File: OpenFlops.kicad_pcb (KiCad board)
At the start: 2 copper layers, 112 x 59.3 mm, 74 parts, among them P1 FLOPPY_CONN, P2 POWER_INPUT, P3 USB_A_FEMALE, P4 PROG_PORT, P5 JUMPERS, P6 ENCODER_PORT, P7 DISPLAY_PORT, Q1 MOS_N_GSD, Q2 MOS_N_GSD, Q3 MOS_N_GSD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

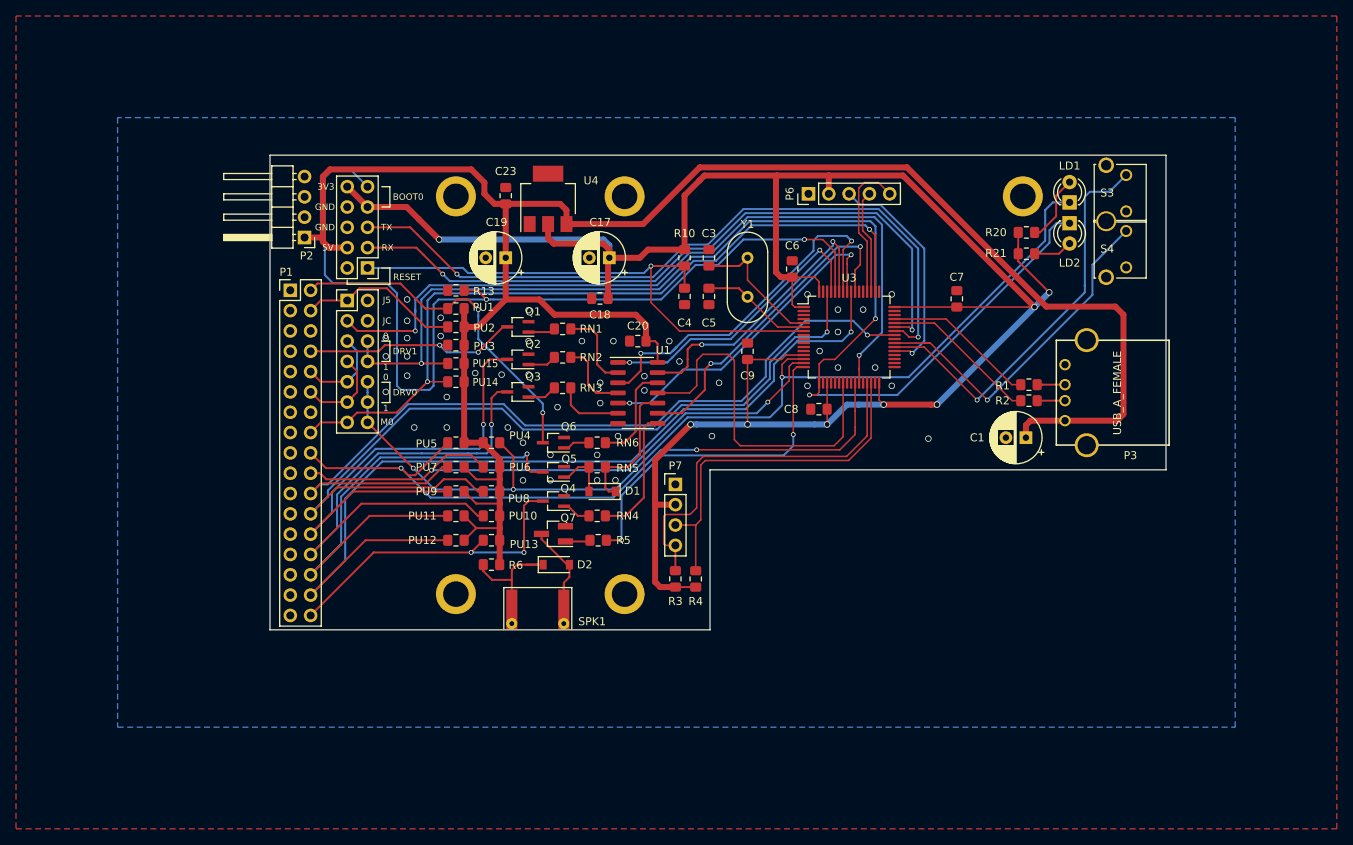
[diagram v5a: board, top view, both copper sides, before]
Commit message: Add P6/P7 pin names
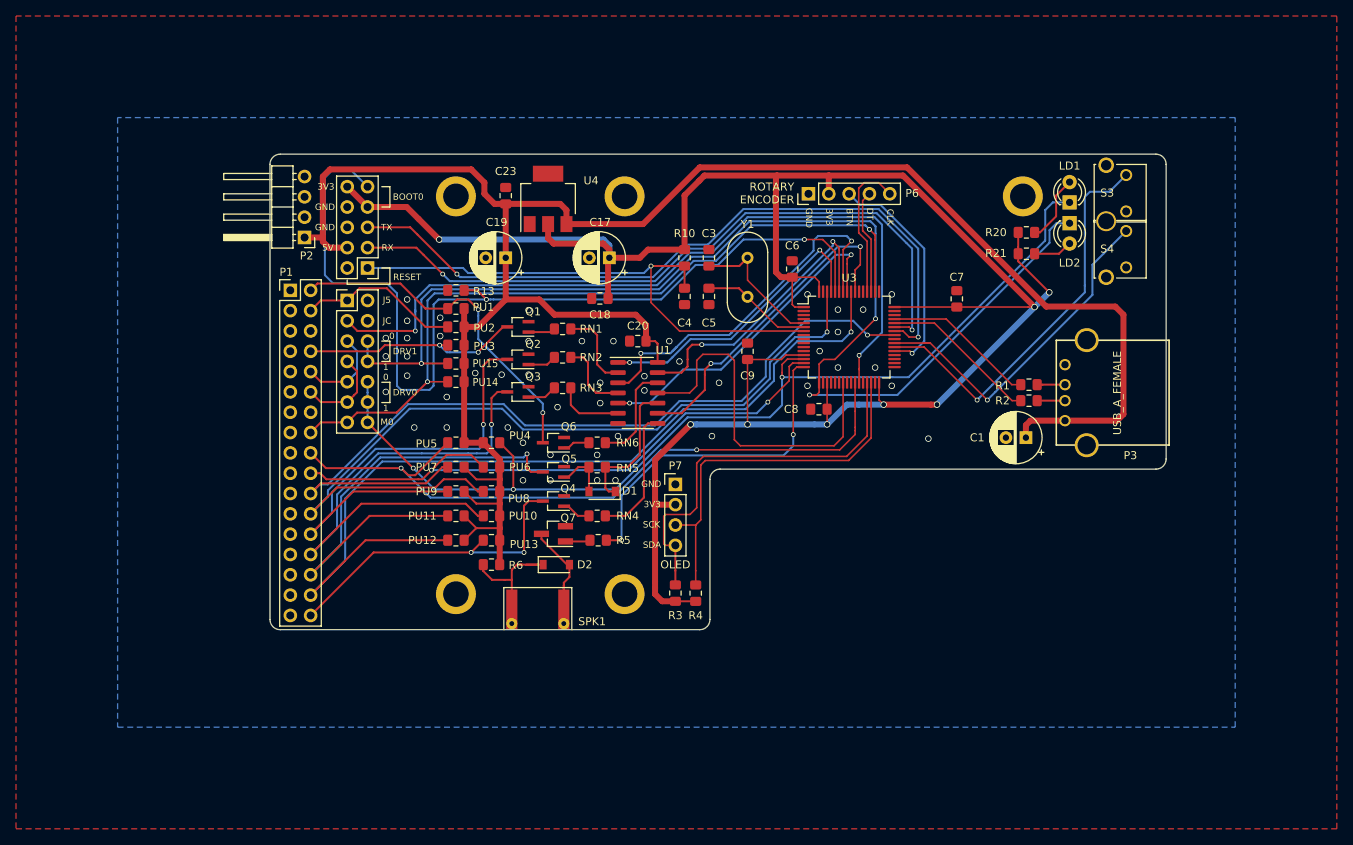
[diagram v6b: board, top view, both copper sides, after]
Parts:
- moved R3 1.78 mm to (145.9, 110.2)
- moved R4 1.78 mm to (148.5, 110.2)
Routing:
- net /disp_clk: track 45.6 -> 47.4 mm
- net /disp_dio: track 47.7 -> 49.5 mm
- net +3V3: track 280.2 -> 281.7 mm
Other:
- board size 112 x 59.3 mm -> 112 x 59.4 mm
- board text added: "BTN"
- board text added: "CLK"
- board text added: "DT"
- board text added: "OLED"
- board text added: "ROTARY ENCODER"
- board text added: "SCK"
- board text added: "SDA"
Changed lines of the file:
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@@
   (general
     (thickness 1.6)
-    (drawings 39)
-    (tracks 823)
+    (drawings 57)
+    (tracks 826)
     (zones 0)
     (modules 74)
@@
     (user_trace_width 0.25)
     (trace_clearance 0.25)
-    (zone_clearance 0.000254)
+    (zone_clearance 0.254)
     (zone_45_only no)
     (trace_min 0.16)
@@
     (tags SOD-123)
     (attr smd)
-    (fp_text reference D1 (at -3.81 0.066668) (layer F.SilkS)
+    (fp_text reference D1 (at -3.439 0.066668) (layer F.SilkS)
       (effects (font (size 1 1) (thickness 0.15)))
     )
@@
   )
   (module Resistor_SMD:R_0805_2012Metric_Pad1.15x1.40mm_HandSolder (layer F.Cu)
-    (at 145.923 108.458 90)
+    (at 145.923 110.236 90)
     (descr "Resistor SMD 0805 (2012 Metric), square (rectangular) end terminal, IPC_7351 nominal with elongated pad for handsoldering. (Body size source: https://docs.google.com/spreadsheets/d/1BsfQQcO9C6DZCsRaXUlFlo91Tg2WpOkGARC1WS5S8t0/edit?usp=sharing), generated with kicad-footprint-generator")
     (tags "resistor handsolder")
@@
   )
   (module Resistor_SMD:R_0805_2012Metric_Pad1.15x1.40mm_HandSolder (layer F.Cu)
-    (at 148.463 108.467 90)
+    (at 148.463 110.245 90)
     (descr "Resistor SMD 0805 (2012 Metric), square (rectangular) end terminal, IPC_7351 nominal with elongated pad for handsoldering. (Body size source: https://docs.google.com/spreadsheets/d/1BsfQQcO9C6DZCsRaXUlFlo91Tg2WpOkGARC1WS5S8t0/edit?usp=sharing), generated with kicad-footprint-generator")
     (tags "resistor handsolder")
@@
     (descr "Through hole straight pin header, 1x05, 2.54mm pitch, single row")
     (tags "Through hole pin header THT 1x05 2.54mm single row")
-    (fp_text reference P6 (at 0 -2.33 90) (layer F.SilkS)
+    (fp_text reference P6 (at 0.0675 12.954 180) (layer F.SilkS)
       (effects (font (size 1 1) (thickness 0.15)))
     )
@@
     )
   )
+  (gr_text OLED (at 145.923 106.68) (layer F.SilkS)
+    (effects (font (size 1 1) (thickness 0.15)))
+  )
+  (gr_text "ROTARY\nENCODER" (at 160.782 60.2575) (layer F.SilkS)
+    (effects (font (size 1 1) (thickness 0.15)) (justify right))
+  )
+  (gr_text SDA (at 143.002 104.213) (layer F.SilkS)
+    (effects (font (size 0.8 0.8) (thickness 0.12)))
+  )
+  (gr_text SCK (at 142.944857 101.673) (layer F.SilkS)
+    (effects (font (size 0.8 0.8) (thickness 0.12)))
+  )
+  (gr_text 3V3 (at 143.021048 99.133) (layer F.SilkS)
+    (effects (font (size 0.8 0.8) (thickness 0.12)))
+  )
+  (gr_text GND (at 142.906762 96.593) (layer F.SilkS)
+    (effects (font (size 0.8 0.8) (thickness 0.12)))
+  )
+  (gr_text GND (at 162.614 63.341238 270) (layer F.SilkS)
+    (effects (font (size 0.8 0.8) (thickness 0.12)))
+  )
+  (gr_text 3V3 (at 165.154 63.226953 270) (layer F.SilkS)
+    (effects (font (size 0.8 0.8) (thickness 0.12)))
+  )
+  (gr_text BTN (at 167.694 63.246 270) (layer F.SilkS)
+    (effects (font (size 0.8 0.8) (thickness 0.12)))
+  )
+  (gr_text DT (at 170.234 62.826953 270) (layer F.SilkS)
+    (effects (font (size 0.8 0.8) (thickness 0.12)))
+  )
+  (gr_text CLK (at 172.774 63.246 270) (layer F.SilkS)
+    (effects (font (size 0.8 0.8) (thickness 0.12)))
+  )
+  (gr_arc (start 151.511 96.012) (end 151.511 94.742) (angle -90) (layer Edge.Cuts) (width 0.05))
+  (gr_arc (start 96.52 113.538) (end 95.25 113.538) (angle -90) (layer Edge.Cuts) (width 0.05))
+  (gr_arc (start 148.971 113.538) (end 148.971 114.808) (angle -90) (layer Edge.Cuts) (width 0.05))
+  (gr_arc (start 205.994 93.472) (end 205.994 94.742) (angle -90) (layer Edge.Cuts) (width 0.05))
+  (gr_arc (start 205.994 56.642) (end 207.264 56.642) (angle -90) (layer Edge.Cuts) (width 0.05))
+  (gr_arc (start 96.52 56.642) (end 96.52 55.372) (angle -90) (layer Edge.Cuts) (width 0.05))
+  (dimension 112.014 (width 0.15) (layer F.Fab)
+    (gr_text "112,014 mm" (at 151.257 43.022994) (layer F.Fab)
+      (effects (font (size 1 1) (thickness 0.15)))
+    )
+    (feature1 (pts (xy 207.264 55.372) (xy 207.264 43.736573)))
+    (feature2 (pts (xy 95.25 55.372) (xy 95.25 43.736573)))
+    (crossbar (pts (xy 95.25 44.322994) (xy 207.264 44.322994)))
+    (arrow1a (pts (xy 207.264 44.322994) (xy 206.137496 44.909415)))
+    (arrow1b (pts (xy 207.264 44.322994) (xy 206.137496 43.736573)))
+    (arrow2a (pts (xy 95.25 44.322994) (xy 96.376504 44.909415)))
+    (arrow2b (pts (xy 95.25 44.322994) (xy 96.376504 43.736573)))
+  )
   (gr_text M0 (at 109.874238 88.846) (layer F.SilkS)
     (effects (font (size 0.8 0.8) (thickness 0.12)))
@@
     (effects (font (size 0.8 0.8) (thickness 0.12)))
   )
-  (gr_text 0 (at 109.728 78.105) (layer F.SilkS)
+  (gr_text 0 (at 110.49 78.105) (layer F.SilkS)
     (effects (font (size 0.8 0.8) (thickness 0.12)))
   )
@@
     (effects (font (size 0.8 0.8) (thickness 0.12)))
   )
-  (gr_line (start 150.25 94.828) (end 207.25 94.828) (layer Edge.Cuts) (width 0.05))
-  (gr_line (start 150.25 114.828) (end 150.25 94.828) (layer Edge.Cuts) (width 0.05))
-  (gr_line (start 95.25 114.828) (end 150.25 114.828) (layer Edge.Cuts) (width 0.05))
-  (gr_line (start 207.25 55.5) (end 207.25 94.828) (layer Edge.Cuts) (width 0.05))
-  (gr_line (start 95.25 55.5) (end 207.25 55.5) (layer Edge.Cuts) (width 0.05))
-  (gr_line (start 95.25 55.5) (end 95.25 114.828) (layer Edge.Cuts) (width 0.05))
+  (gr_line (start 151.511 94.742) (end 205.994 94.742) (layer Edge.Cuts) (width 0.05))
+  (gr_line (start 150.241 113.538) (end 150.241 96.012) (layer Edge.Cuts) (width 0.05))
+  (gr_line (start 96.52 114.808) (end 148.971 114.808) (layer Edge.Cuts) (width 0.05))
+  (gr_line (start 207.264 56.642) (end 207.264 93.472) (layer Edge.Cuts) (width 0.05))
+  (gr_line (start 96.52 55.372) (end 205.994 55.372) (layer Edge.Cuts) (width 0.05))
+  (gr_line (start 95.25 56.642) (end 95.25 113.538) (layer Edge.Cuts) (width 0.05))
   (via (at 177.546 90.932) (size 0.8) (drill 0.6) (layers F.Cu B.Cu) (net 1))
   (via (at 124.968 89.535) (size 0.8) (drill 0.6) (layers F.Cu B.Cu) (net 1))
@@
   (via (at 120.904 82.733806) (size 0.8) (drill 0.6) (layers F.Cu B.Cu) (net 1))
   (via (at 109.728 85.09) (size 0.8) (drill 0.6) (layers F.Cu B.Cu) (net 1))
-  (via (at 116.586 75.819) (size 0.8) (drill 0.6) (layers F.Cu B.Cu) (net 1))
-  (via (at 116.586 78.105) (size 0.8) (drill 0.6) (layers F.Cu B.Cu) (net 1))
+  (via (at 116.5225 75.819) (size 0.8) (drill 0.6) (layers F.Cu B.Cu) (net 1))
+  (via (at 116.5225 78.105) (size 0.8) (drill 0.6) (layers F.Cu B.Cu) (net 1))
   (via (at 112.395 73.533) (size 0.8) (drill 0.6) (layers F.Cu B.Cu) (net 1))
   (via (at 112.395 76.2) (size 0.8) (drill 0.6) (layers F.Cu B.Cu) (net 1))
@@
   (segment (start 104.902 59.436) (end 107.442 61.976) (width 0.75) (layer F.Cu) (net 5))
   (segment (start 143.383 93.599) (end 143.383 98.425) (width 0.75) (layer F.Cu) (net 5))
-  (segment (start 148.454 109.483) (end 148.463 109.492) (width 0.25) (layer F.Cu) (net 5))
-  (segment (start 145.923 109.483) (end 148.454 109.483) (width 0.25) (layer F.Cu) (net 5))
-  (segment (start 144.027 109.483) (end 145.923 109.483) (width 0.75) (layer F.Cu) (net 5))
-  (segment (start 143.383 108.839) (end 144.027 109.483) (width 0.75) (layer F.Cu) (net 5))
   (segment (start 143.383 99.187) (end 145.923 99.187) (width 0.75) (layer F.Cu) (net 5))
   (segment (start 143.383 98.425) (end 143.383 99.187) (width 0.75) (layer F.Cu) (net 5))
@@
   (via (at 178.6255 86.6775) (size 0.8) (drill 0.6) (layers F.Cu B.Cu) (net 5))
   (segment (start 177.8635 86.6775) (end 178.6255 86.6775) (width 0.75) (layer F.Cu) (net 5))
+  (segment (start 145.923 111.261) (end 148.333593 111.261) (width 0.25) (layer F.Cu) (net 5))
+  (segment (start 143.383 109.601) (end 143.383 110.363) (width 0.75) (layer F.Cu) (net 5))
+  (segment (start 143.383 108.839) (end 143.383 109.601) (width 0.75) (layer F.Cu) (net 5))
+  (segment (start 144.281 111.261) (end 145.923 111.261) (width 0.75) (layer F.Cu) (net 5))
+  (segment (start 143.383 110.363) (end 144.281 111.261) (width 0.75) (layer F.Cu) (net 5))
   (segment (start 123.961 93.49) (end 121.911 91.44) (width 0.75) (layer F.Cu) (net 6))
   (segment (start 123.961 94.488) (end 123.961 93.49) (width 0.75) (layer F.Cu) (net 6))
@@
   (segment (start 149.098 94.234) (end 149.6695 93.6625) (width 0.2) (layer F.Cu) (net 9))
   (segment (start 148.463 101.727) (end 149.098 101.092) (width 0.2) (layer F.Cu) (net 9))
+  (segment (start 148.463 107.442) (end 148.463 109.22) (width 0.2) (layer F.Cu) (net 9))
   (segment (start 145.923 104.267) (end 145.923 107.433) (width 0.25) (layer F.Cu) (net 10))
   (segment (start 167.3225 93.1545) (end 169.89 90.587) (width 0.2) (layer F.Cu) (net 10))
@@
   (segment (start 144.4625 100.6475) (end 144.697999 100.412001) (width 0.2) (layer F.Cu) (net 10))
   (segment (start 144.697999 100.412001) (end 147.745999 100.412001) (width 0.2) (layer F.Cu) (net 10))
+  (segment (start 145.923 107.433) (end 145.923 109.211) (width 0.25) (layer F.Cu) (net 10))
   (via (at 125.6665 97.282) (size 0.6) (drill 0.4) (layers F.Cu B.Cu) (net 11))
   (via (at 113.157 94.615) (size 0.6) (drill 0.4) (layers F.Cu B.Cu) (net 11))
@@
     (connect_pads (clearance 0.254))
     (min_thickness 0.0254)
-    (fill yes (arc_segments 32) (thermal_gap 0.508) (thermal_bridge_width 0.508))
+    (fill (arc_segments 32) (thermal_gap 0.254) (thermal_bridge_width 0.508))
     (polygon
       (pts
@@
     (connect_pads (clearance 0.254))
     (min_thickness 0.0254)
-    (fill yes (arc_segments 32) (thermal_gap 0.508) (thermal_bridge_width 0.508))
+    (fill (arc_segments 32) (thermal_gap 0.254) (thermal_bridge_width 0.508))
     (polygon
       (pts

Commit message: 74HC04 -> 74HCT04
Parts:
- U1: value 74HC04 -> 74HCT04
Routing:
- net GND: vias 49 -> 55
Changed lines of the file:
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@@
   (general
     (thickness 1.6)
-    (drawings 57)
-    (tracks 826)
+    (drawings 60)
+    (tracks 832)
     (zones 0)
     (modules 74)
@@
       (effects (font (size 1 1) (thickness 0.15)))
     )
-    (fp_text value 74HC04 (at 0 5.28) (layer F.Fab)
+    (fp_text value 74HCT04 (at 0 5.28) (layer F.Fab)
       (effects (font (size 1 1) (thickness 0.15)))
     )
@@
     )
   )
+  (dimension 39.37 (width 0.15) (layer F.Fab)
+    (gr_text "39,370 mm" (at 212.755 75.057 270) (layer F.Fab)
+      (effects (font (size 1 1) (thickness 0.15)))
+    )
+    (feature1 (pts (xy 207.264 94.742) (xy 212.041421 94.742)))
+    (feature2 (pts (xy 207.264 55.372) (xy 212.041421 55.372)))
+    (crossbar (pts (xy 211.455 55.372) (xy 211.455 94.742)))
+    (arrow1a (pts (xy 211.455 94.742) (xy 210.868579 93.615496)))
+    (arrow1b (pts (xy 211.455 94.742) (xy 212.041421 93.615496)))
+    (arrow2a (pts (xy 211.455 55.372) (xy 210.868579 56.498504)))
+    (arrow2b (pts (xy 211.455 55.372) (xy 212.041421 56.498504)))
+  )
+  (dimension 20.066 (width 0.15) (layer F.Fab)
+    (gr_text "20,066 mm" (at 158.907 104.775 270) (layer F.Fab)
+      (effects (font (size 1 1) (thickness 0.15)))
+    )
+    (feature1 (pts (xy 150.241 114.808) (xy 158.193421 114.808)))
+    (feature2 (pts (xy 150.241 94.742) (xy 158.193421 94.742)))
+    (crossbar (pts (xy 157.607 94.742) (xy 157.607 114.808)))
+    (arrow1a (pts (xy 157.607 114.808) (xy 157.020579 113.681496)))
+    (arrow1b (pts (xy 157.607 114.808) (xy 158.193421 113.681496)))
+    (arrow2a (pts (xy 157.607 94.742) (xy 157.020579 95.868504)))
+    (arrow2b (pts (xy 157.607 94.742) (xy 158.193421 95.868504)))
+  )
+  (dimension 59.436 (width 0.15) (layer F.Fab)
+    (gr_text "59,436 mm" (at 84.806 85.09 270) (layer F.Fab)
+      (effects (font (size 1 1) (thickness 0.15)))
+    )
+    (feature1 (pts (xy 95.25 114.808) (xy 85.519579 114.808)))
+    (feature2 (pts (xy 95.25 55.372) (xy 85.519579 55.372)))
+    (crossbar (pts (xy 86.106 55.372) (xy 86.106 114.808)))
+    (arrow1a (pts (xy 86.106 114.808) (xy 85.519579 113.681496)))
+    (arrow1b (pts (xy 86.106 114.808) (xy 86.692421 113.681496)))
+    (arrow2a (pts (xy 86.106 55.372) (xy 85.519579 56.498504)))
+    (arrow2b (pts (xy 86.106 55.372) (xy 86.692421 56.498504)))
+  )
   (gr_text OLED (at 145.923 106.68) (layer F.SilkS)
     (effects (font (size 1 1) (thickness 0.15)))
@@
     (effects (font (size 1 1) (thickness 0.15)) (justify mirror))
   )
-  (gr_text github.com/SukkoPera/OpenFlops (at 125.984 101.346) (layer B.SilkS)
+  (gr_text github.com/SukkoPera/OpenFlops (at 123.063 100.457) (layer B.SilkS)
     (effects (font (size 1 1) (thickness 0.15)) (justify mirror))
   )
-  (gr_text "Licensed under CERN OHL v.1.2" (at 125.984 104.14) (layer B.SilkS)
+  (gr_text "Licensed under CERN OHL v.1.2" (at 123.063 103.251) (layer B.SilkS)
     (effects (font (size 1 1) (thickness 0.15)) (justify mirror))
   )
@@
   (via (at 150.495 90.6145) (size 0.8) (drill 0.6) (layers F.Cu B.Cu) (net 1))
   (via (at 151.384 83.947) (size 0.8) (drill 0.6) (layers F.Cu B.Cu) (net 1))
+  (via (at 104.902 92.71) (size 0.8) (drill 0.6) (layers F.Cu B.Cu) (net 1))
+  (via (at 102.616 90.17) (size 0.8) (drill 0.6) (layers F.Cu B.Cu) (net 1))
+  (via (at 102.616 81.28) (size 0.8) (drill 0.6) (layers F.Cu B.Cu) (net 1))
+  (via (at 102.616 85.09) (size 0.8) (drill 0.6) (layers F.Cu B.Cu) (net 1))
+  (via (at 102.616 87.63) (size 0.8) (drill 0.6) (layers F.Cu B.Cu) (net 1))
+  (via (at 102.616 76.835) (size 0.8) (drill 0.6) (layers F.Cu B.Cu) (net 1))
   (segment (start 153.915 69.351) (end 154.94 68.326) (width 0.25) (layer F.Cu) (net 2))
   (segment (start 150.114 69.351) (end 153.915 69.351) (width 0.25) (layer F.Cu) (net 2))
@@
     (connect_pads (clearance 0.254))
     (min_thickness 0.0254)
-    (fill (arc_segments 32) (thermal_gap 0.254) (thermal_bridge_width 0.508))
+    (fill yes (arc_segments 32) (thermal_gap 0.254) (thermal_bridge_width 0.508))
     (polygon
       (pts
@@
     (connect_pads (clearance 0.254))
     (min_thickness 0.0254)
-    (fill (arc_segments 32) (thermal_gap 0.254) (thermal_bridge_width 0.508))
+    (fill yes (arc_segments 32) (thermal_gap 0.254) (thermal_bridge_width 0.508))
     (polygon
       (pts

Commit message: Some refinements
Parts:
- moved R5 0.13 mm to (136.1, 103.6)
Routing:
- net /~selx: track 126.6 -> 123.6 mm
- net /dir: track 88.1 -> 86.6 mm
- net /boot0: track 117.8 -> 118.9 mm
- net GND: vias 55 -> 79
